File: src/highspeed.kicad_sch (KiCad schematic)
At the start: 4 parts, among them J3 USB_C_Receptacle, J4 USB3_A, J5 HDMI_A_1.4

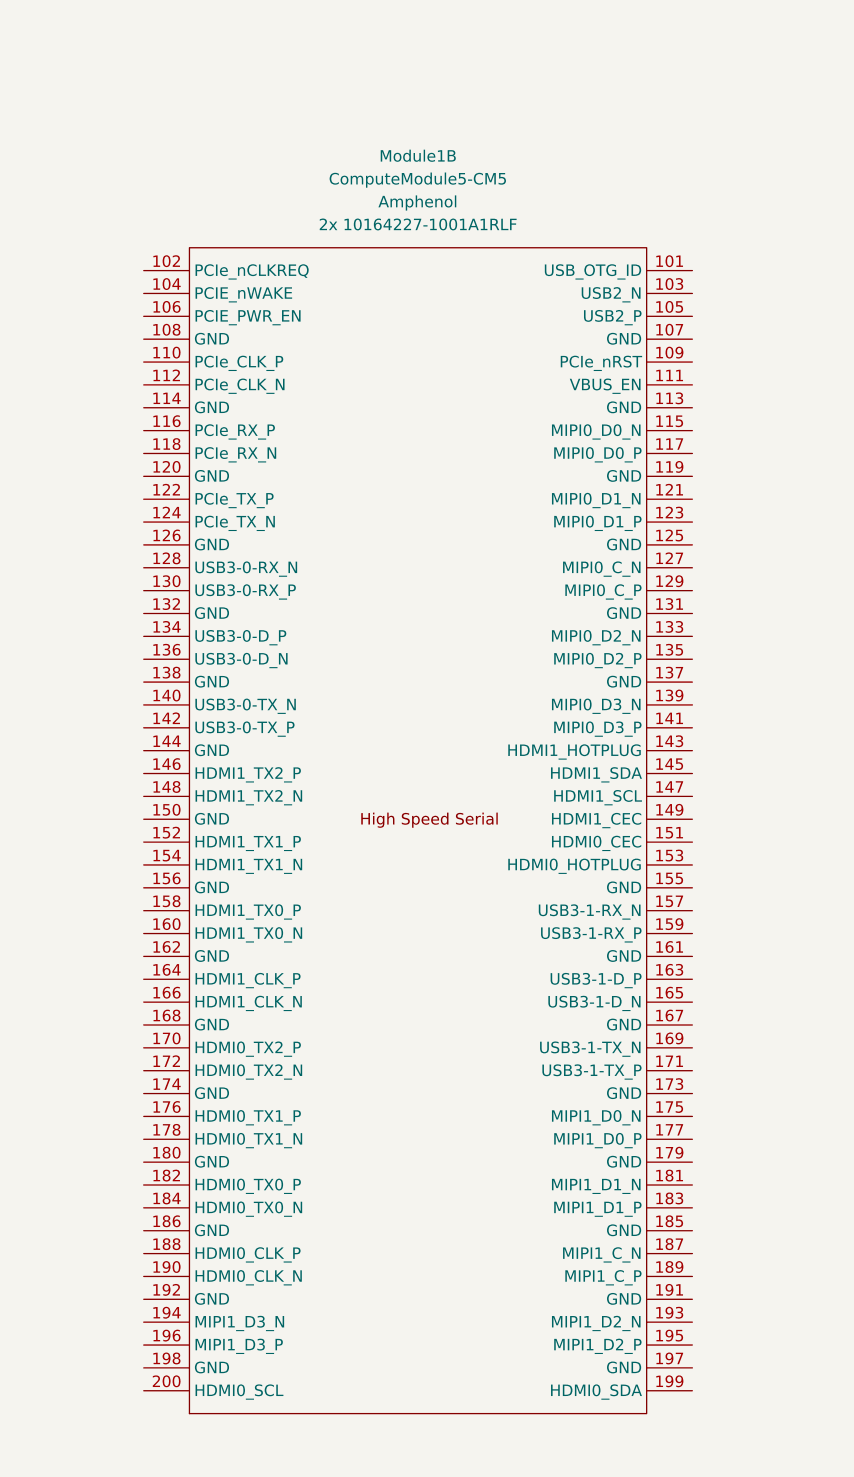
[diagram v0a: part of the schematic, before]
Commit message: Add ethernet circuitry
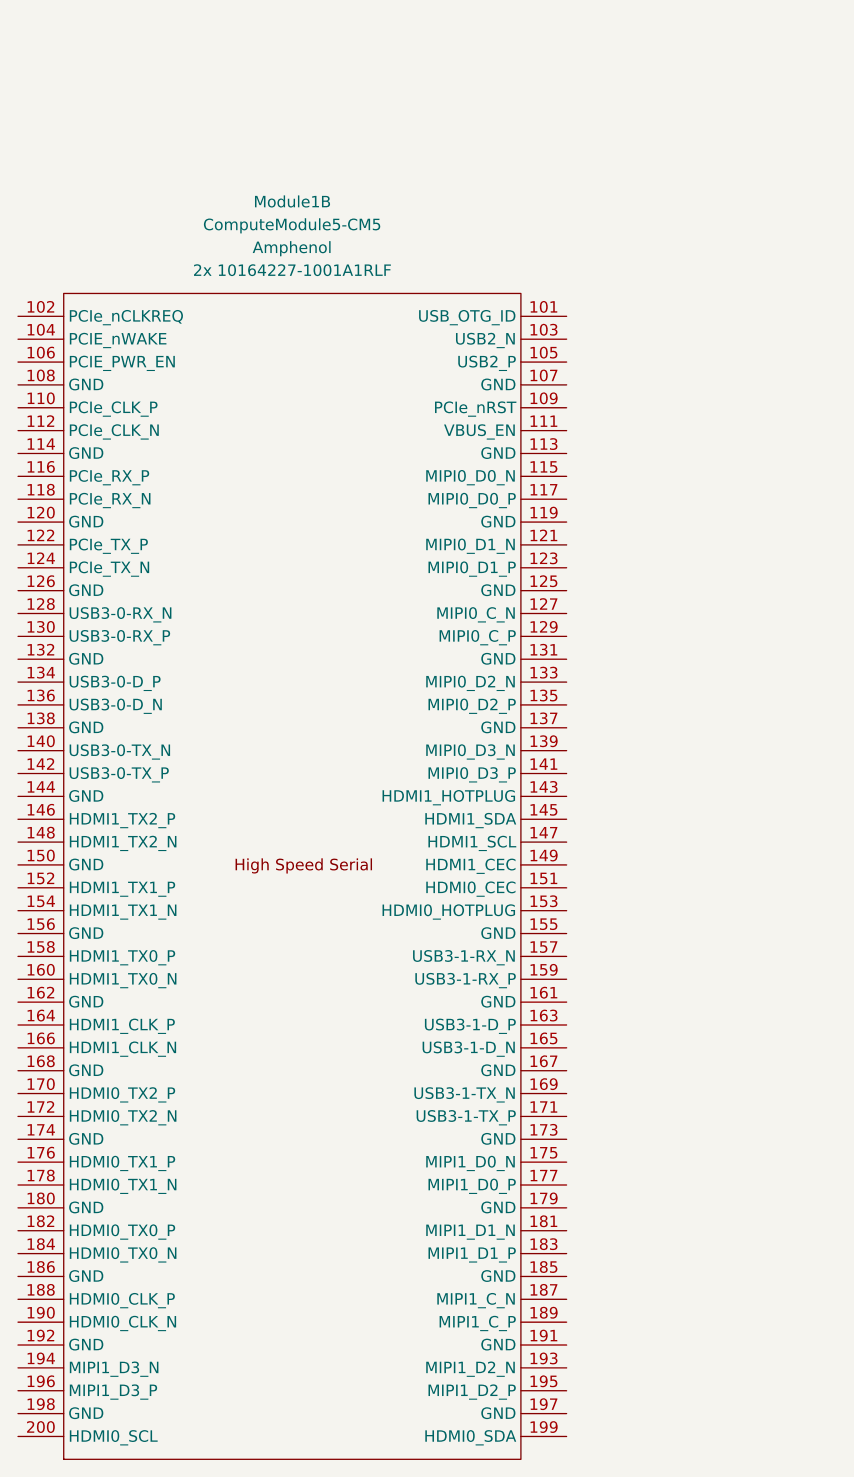
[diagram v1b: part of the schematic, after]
